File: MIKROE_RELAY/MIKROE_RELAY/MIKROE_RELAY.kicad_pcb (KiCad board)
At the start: 2 copper layers, 32.7 x 53.5 mm, 24 parts, among them J1 RELAY1, J2 RELAY2, J3 Screw_Terminal_01x04, K1 SRD-05VDC-SL-C, K2 SRD-05VDC-SL-C, Q1 Q_NMOS_Depletion_GSD, Q2 Q_NMOS_Depletion_GSD, U2 B0505S-2WR3, U3 PC817, U4 PC817

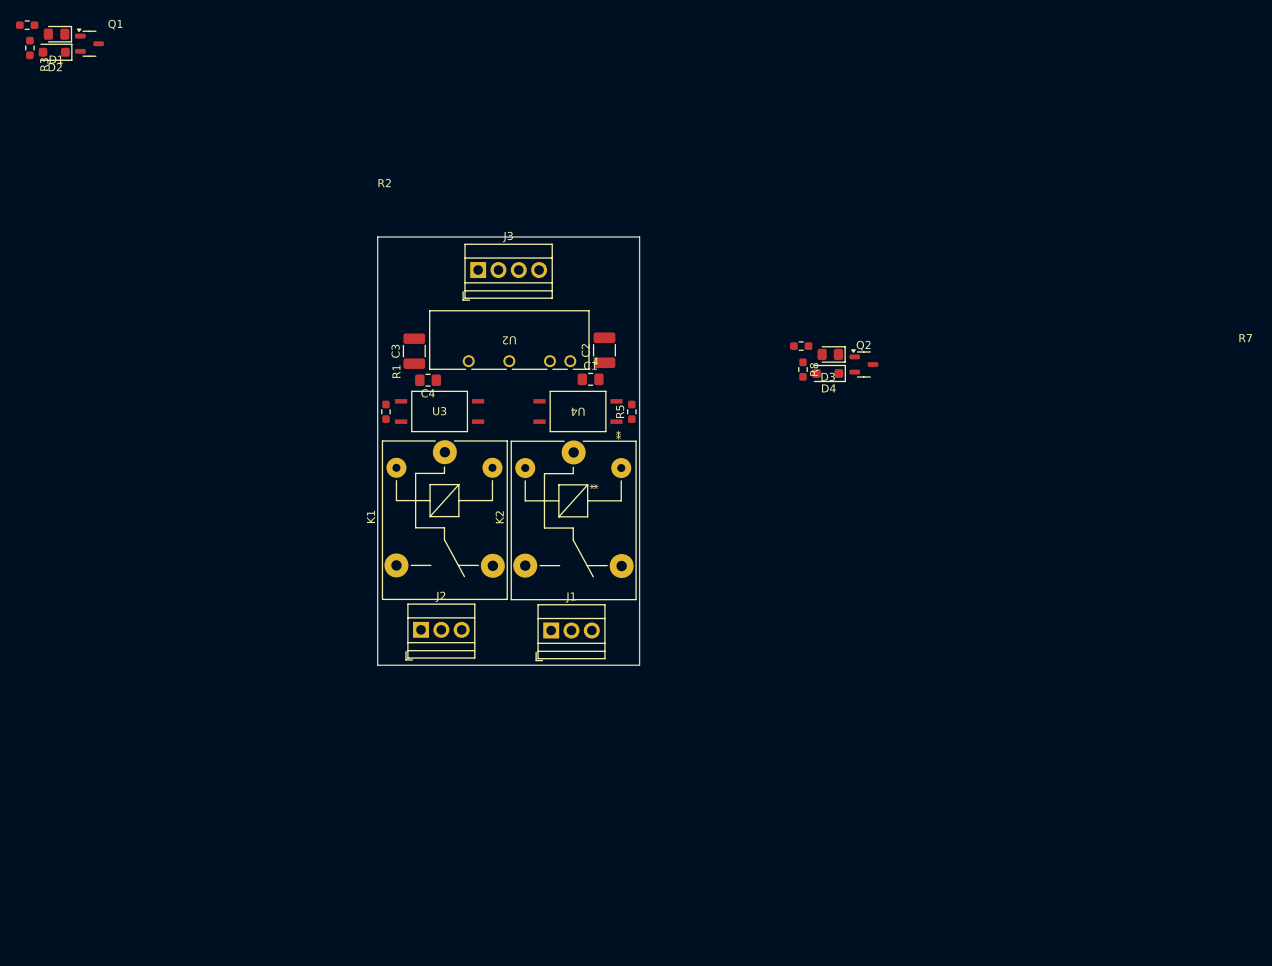
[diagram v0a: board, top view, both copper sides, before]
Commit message: -relay update traces
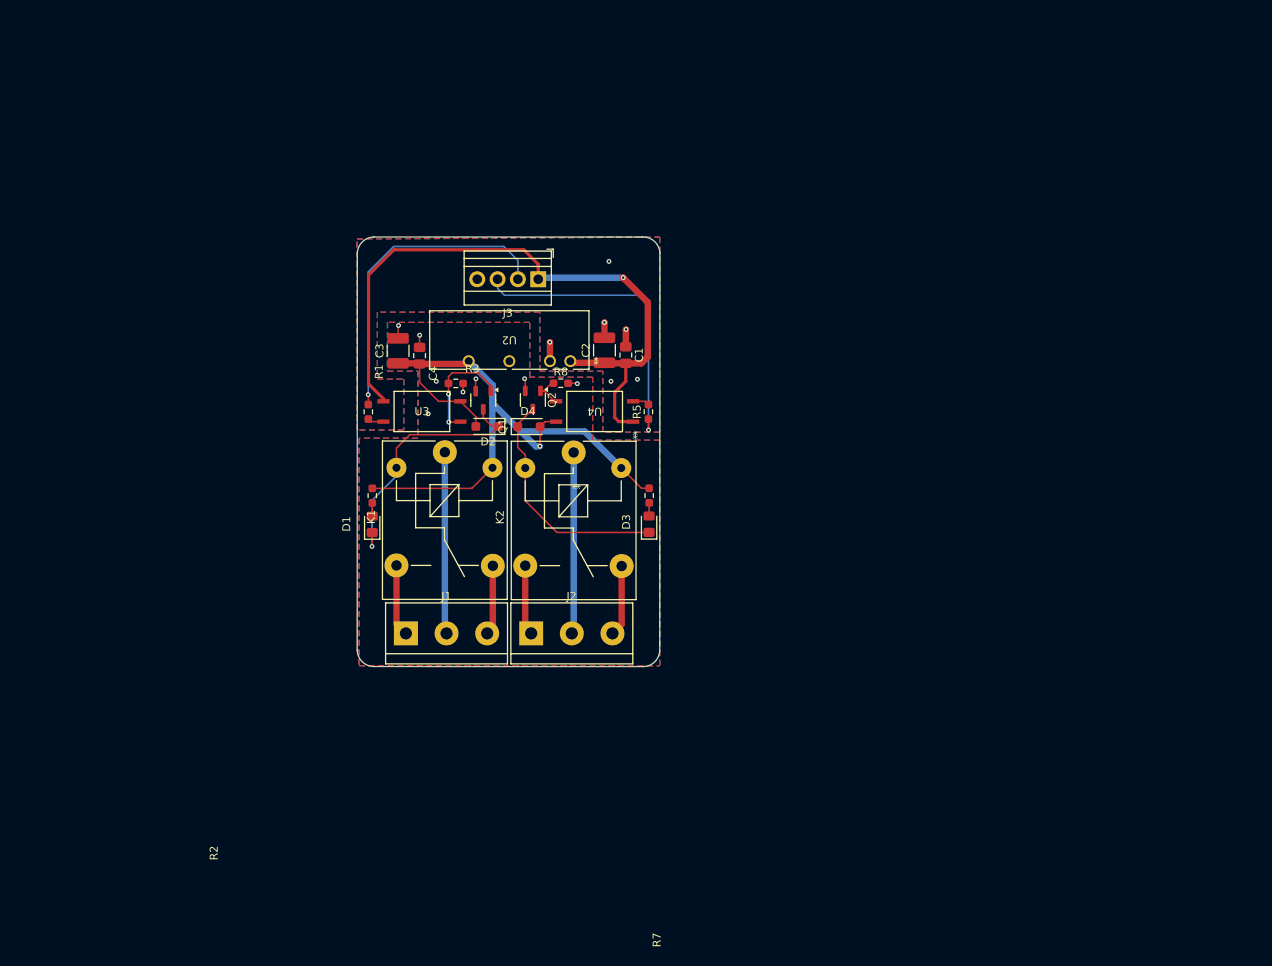
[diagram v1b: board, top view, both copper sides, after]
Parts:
- J1, J2: footprint TerminalBlock:TerminalBlock_Xinya_XY308-2.54-3P_1x03_P2.54mm_Horizontal -> TerminalBlock:TerminalBlock_bornier-3_P5.08mm
- moved R2 72.9 mm to (107.8, 69.2), turned to -90 degrees
- moved D1 72.9 mm to (107.8, 72.8), turned to 90 degrees
- moved D2 71.5 mm to (122.2, 60.5)
- moved R3 67.8 mm to (118.3, 55.1), turned to 0 degrees
- moved Q1 66.4 mm to (121.7, 57.2), turned to -90 degrees
- moved Q2 41.6 mm to (127.9, 57.2), turned to -90 degrees
- moved D4 37.9 mm to (127.4, 60.5), turned to 0 degrees
- moved D3 31.0 mm to (142.4, 72.7), turned to 90 degrees
- moved R8 30.3 mm to (131.4, 55.1), turned to 0 degrees
- moved R7 26.6 mm to (142.4, 69.2), turned to -90 degrees
- moved J1 18.2 mm to (112.0, 86.4)
- moved J2 13.8 mm to (127.7, 86.4)
- moved J3 7.60 mm to (128.6, 42.1), turned to 180 degrees
- moved C1 5.34 mm to (139.5, 51.6), turned to -90 degrees
- moved C4 3.25 mm to (113.7, 51.7), turned to -90 degrees
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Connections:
- J3 pad 1: GNDD -> 5V_ISO
- J3 pad 2: /RE2 -> /RE1
- J3 pad 3: /RE1 -> /RE2
- J3 pad 4: 5V_ISO -> GNDD
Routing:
- net 5V_RLY: track 0.00 -> 86.2 mm, vias 0 -> 1
- net 5V_ISO: track 0.00 -> 83.9 mm, vias 0 -> 1
- net /RE1: track 0.00 -> 39.7 mm, vias 0 -> 1
- net /RE2: track 0.00 -> 37.9 mm, vias 0 -> 1
- net Net-(D1-K): track 0.00 -> 32.5 mm, vias 0 -> 1
- net Net-(D3-K): track 0.00 -> 29.8 mm
- net COM1: track 0.00 -> 22.7 mm
- net COM2: track 0.00 -> 22.7 mm
- net Net-(Q1-G): track 0.00 -> 14.0 mm, vias 0 -> 2
- net NO1: track 0.00 -> 8.99 mm
- net NC2: track 0.00 -> 8.90 mm
- net NO2: track 0.00 -> 8.78 mm
- net NC1: track 0.00 -> 8.74 mm
- net GNDPWR: track 0.00 -> 8.55 mm, vias 0 -> 8
- net GNDD: track 0.00 -> 6.49 mm, vias 0 -> 6
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- added copper zone on B.Cu, net GNDD
- added copper zone on F.Cu, net GNDD
- added copper zone on B.Cu, net GNDPWR
- added copper zone on F.Cu, net GNDPWR
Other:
- board size 32.7 x 53.5 mm -> 37.8 x 53.7 mm

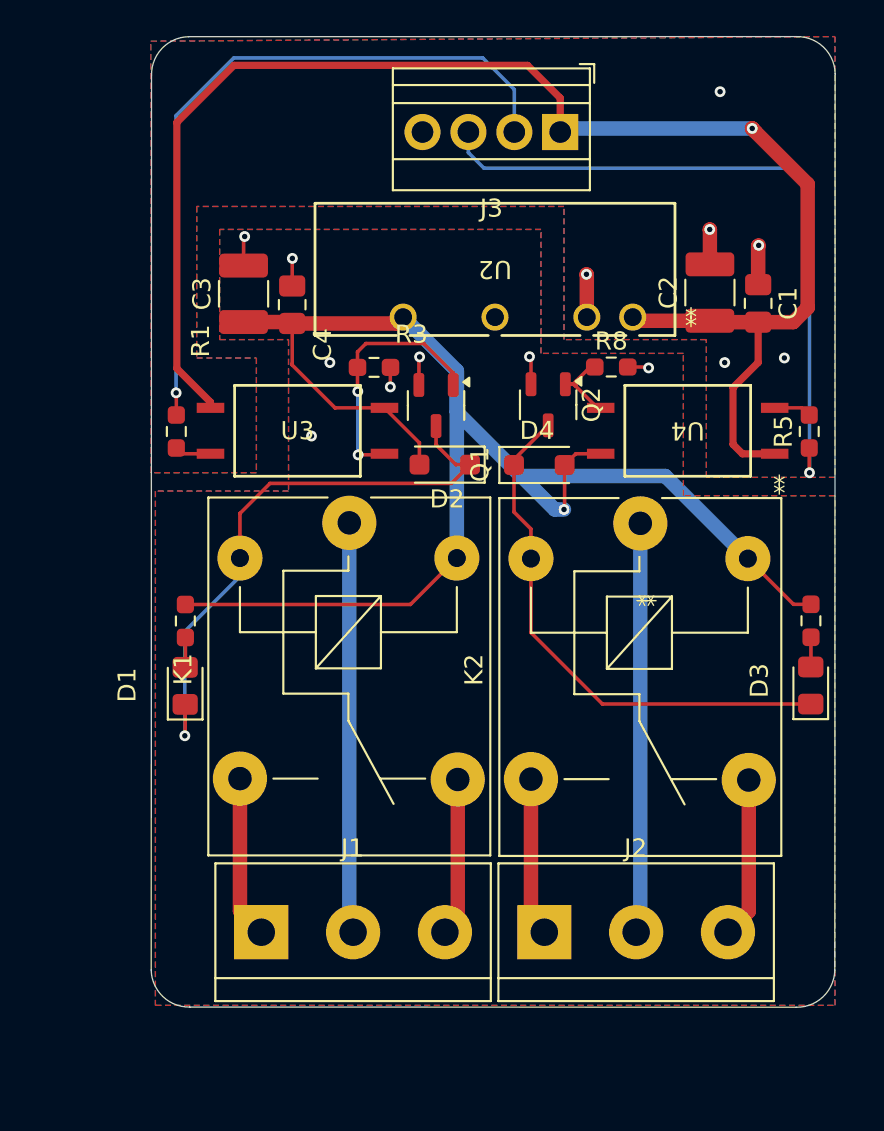
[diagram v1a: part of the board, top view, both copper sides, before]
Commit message: -
updated silk , lacking aesthetic silk
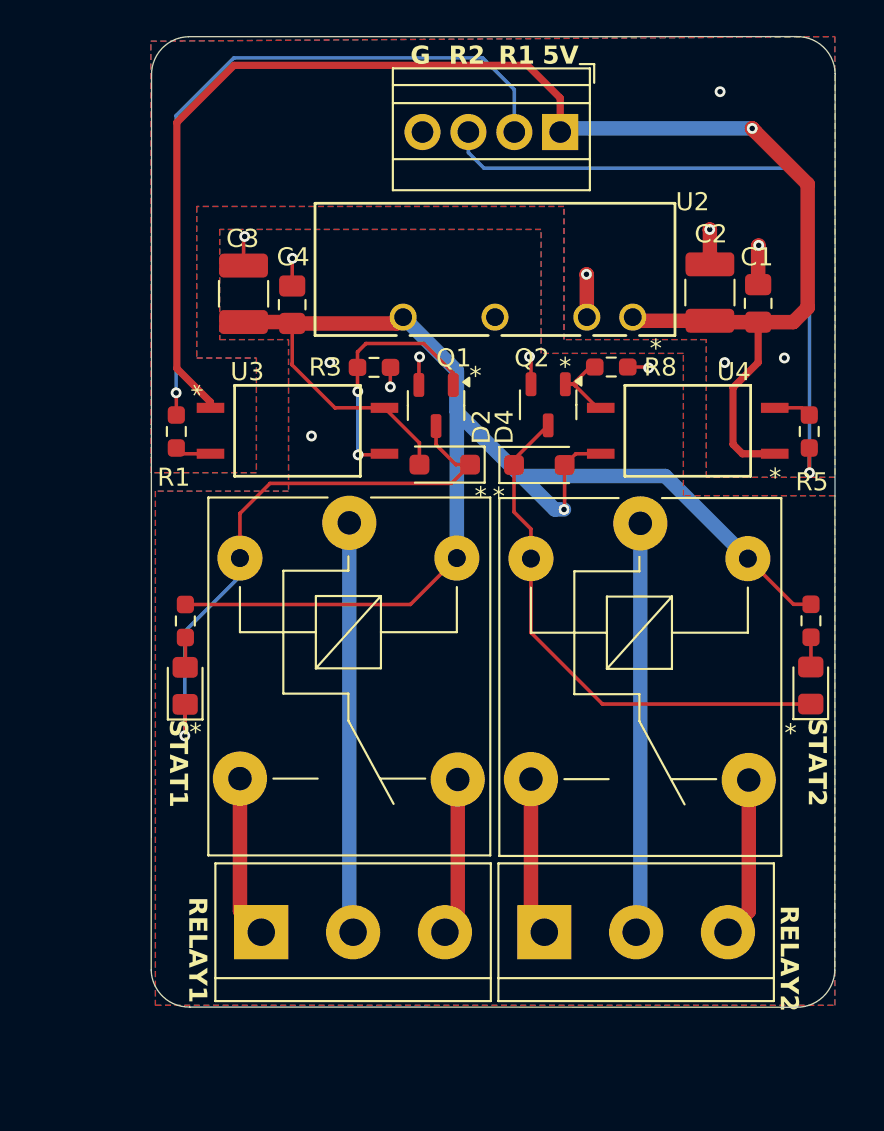
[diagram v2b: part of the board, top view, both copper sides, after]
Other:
- board text added: "*"
- board text added: "5V"
- board text added: "COM1"
- board text added: "COM2"
- board text added: "G"
- board text added: "NC1"
- board text added: "NC2"
- board text added: "NO1"
- board text added: "NO2"
- board text added: "R1"
- board text added: "R2"
- board text added: "RELAY1"
- board text added: "RELAY2"
- board text added: "STAT1"
- board text added: "STAT2"

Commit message: -
updated silk
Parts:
- added G***: LOGO, logo:logo2, F.Cu at (139.5, 48.1)
- added H1: MountingHole, MountingHole:MountingHole_3.2mm_M3_DIN965_Pad, F.Cu at (104.6, 40.1)
- added H2: MountingHole, MountingHole:MountingHole_3.2mm_M3_DIN965_Pad, F.Cu at (145.1, 40.1)
- added H3: MountingHole, MountingHole:MountingHole_3.2mm_M3_DIN965_Pad, F.Cu at (104.6, 87.1)
- added H4: MountingHole, MountingHole:MountingHole_3.2mm_M3_DIN965_Pad, F.Cu at (145.1, 87.1)
- added kibuzzard-6720ECCE: G***, kibuzzard-6720ECCE, F.Cu at (105.7, 77.5)
- added kibuzzard-6720ECE8: G***, kibuzzard-6720ECE8, F.Cu at (144.3, 77.7)
- added kibuzzard-6720EF98: G***, kibuzzard-6720EF98, F.Cu at (125.2, 37.8)
- added kibuzzard-6720F047: G***, kibuzzard-6720F047, B.Cu at (125.2, 37.8)
- added kibuzzard-6720F077: G***, kibuzzard-6720F077, F.Cu at (141.2, 86.3)
- added kibuzzard-6720F077: G***, kibuzzard-6720F077, B.Cu at (141.2, 86.3)
- added kibuzzard-6720F294: G***, kibuzzard-6720F294, F.Cu at (108.6, 86.5)
- added kibuzzard-6720F294: G***, kibuzzard-6720F294, B.Cu at (108.5, 86.5)
- added kibuzzard-6720F424: G***, kibuzzard-6720F424, B.Cu at (112.1, 89.4)
- added kibuzzard-6720F448: G***, kibuzzard-6720F448, B.Cu at (122.3, 89.4)
- added kibuzzard-6720F477: G***, kibuzzard-6720F477, B.Cu at (127.5, 89.4)
- added kibuzzard-6720F484: G***, kibuzzard-6720F484, B.Cu at (138.2, 89.4)
- added kibuzzard-6720F4CB: G***, kibuzzard-6720F4CB, B.Cu at (117.2, 89.4)
- added kibuzzard-6720F4E3: G***, kibuzzard-6720F4E3, B.Cu at (132.9, 89.4)
- added kibuzzard-6720F54C: G***, kibuzzard-6720F54C, F.Cu at (102.5, 72.9)
- added kibuzzard-6720F708: G***, kibuzzard-6720F708, F.Cu at (103.4, 49.0)
- moved R2 2.17 mm to (105.7, 69.2)
- moved D1 2.16 mm to (105.7, 72.8)
- moved D3 1.84 mm to (144.3, 72.7)
- moved R7 1.83 mm to (144.3, 69.2)
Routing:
- net 5V_ISO: track 83.9 -> 79.4 mm
- net 5V_RLY: track 86.2 -> 90.2 mm
- net /RE1: track 39.7 -> 36.5 mm
- net Net-(D3-K): track 29.8 -> 31.6 mm
- net Net-(D1-K): track 32.5 -> 33.6 mm
- net GNDD: vias 6 -> 8
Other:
- board size 37.8 x 53.7 mm -> 47.4 x 53.7 mm
- board text removed: "5V"
- board text removed: "COM1"
- board text removed: "COM2"
- board text removed: "G"
- board text removed: "NC1"
- board text removed: "NC2"
- board text removed: "NO1"
- board text removed: "NO2"
- board text removed: "R1"
- board text removed: "R2"
- board text removed: "RELAY1"
- board text removed: "RELAY2"
- board text removed: "STAT1"
- board text removed: "STAT2"

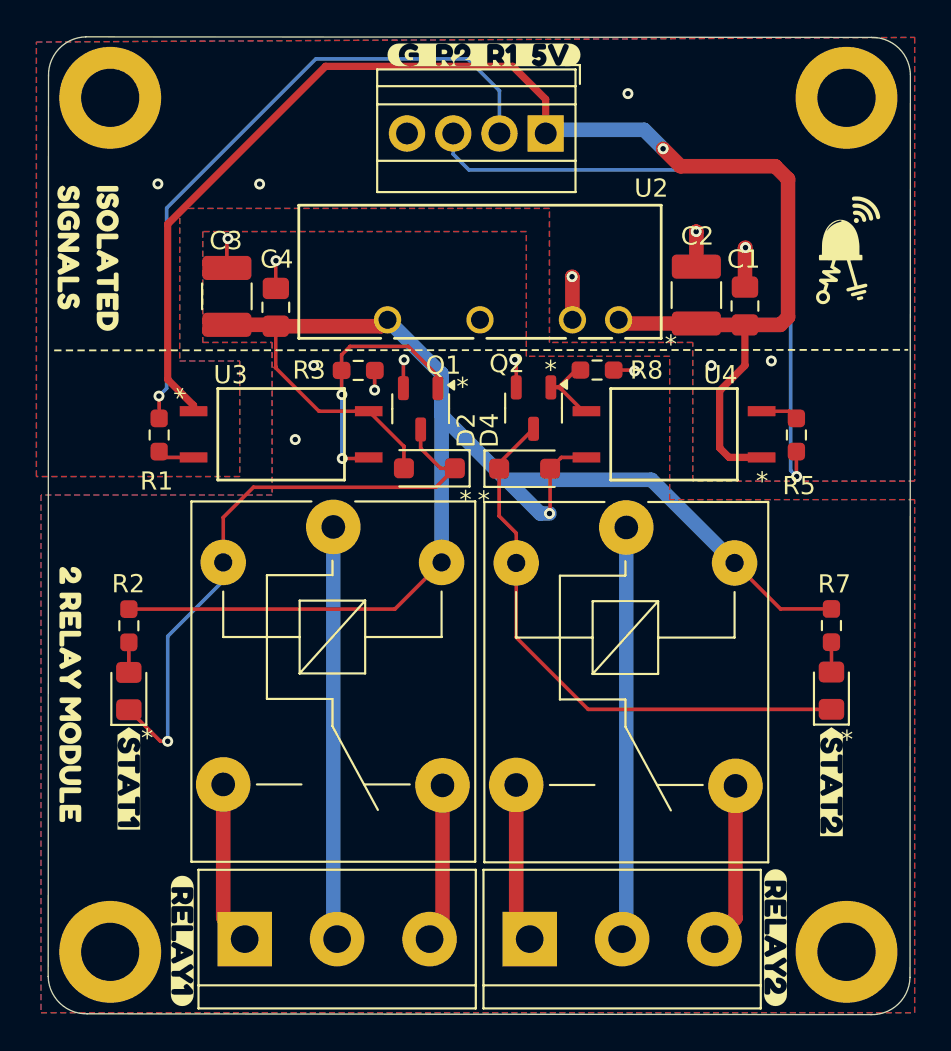
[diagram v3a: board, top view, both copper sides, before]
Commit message: Fixed Silk Screen
Minor Adjustments
1. Silk Screens
2. Swapped Relay Pin Signals
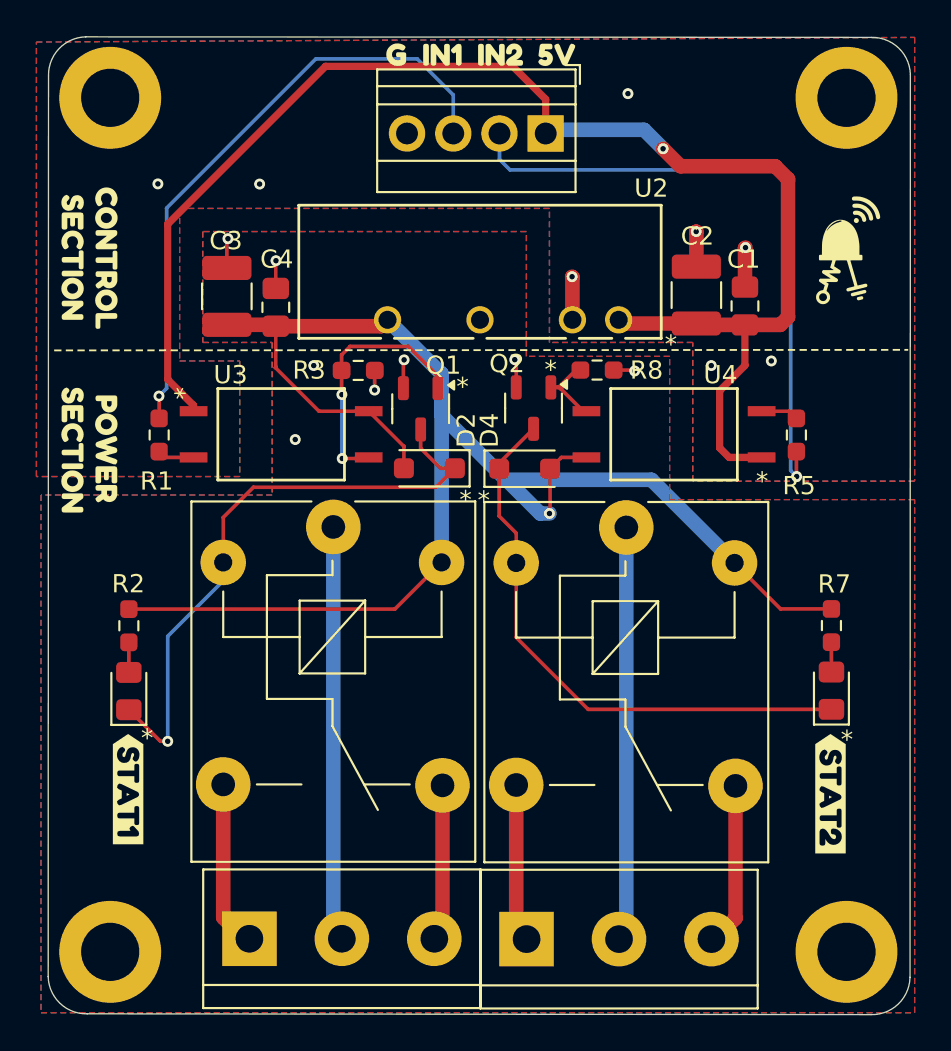
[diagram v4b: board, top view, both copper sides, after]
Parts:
- removed kibuzzard-6720ECCE: G***, kibuzzard-6720ECCE
- removed kibuzzard-6720ECE8: G***, kibuzzard-6720ECE8
- removed kibuzzard-6720EF98: G***, kibuzzard-6720EF98
- removed kibuzzard-6720F047: G***, kibuzzard-6720F047
- removed kibuzzard-6720F077 (x2): G***, kibuzzard-6720F077
- removed kibuzzard-6720F294 (x2): G***, kibuzzard-6720F294
- removed kibuzzard-6720F424: G***, kibuzzard-6720F424
- removed kibuzzard-6720F448: G***, kibuzzard-6720F448
- removed kibuzzard-6720F477: G***, kibuzzard-6720F477
- removed kibuzzard-6720F484: G***, kibuzzard-6720F484
- removed kibuzzard-6720F4CB: G***, kibuzzard-6720F4CB
- removed kibuzzard-6720F4E3: G***, kibuzzard-6720F4E3
- removed kibuzzard-6720F54C: G***, kibuzzard-6720F54C
- removed kibuzzard-6720F708: G***, kibuzzard-6720F708
- added kibuzzard-672479F1: G***, kibuzzard-672479F1, F.Cu at (103.5, 49.0)
- added kibuzzard-67247A26: G***, kibuzzard-67247A26, F.Cu at (103.5, 59.5)
- added kibuzzard-67247B67: G***, kibuzzard-67247B67, F.Cu at (144.2, 78.4)
- added kibuzzard-67247B7C: G***, kibuzzard-67247B7C, F.Cu at (105.6, 78.1)
- added kibuzzard-67247F02: G***, kibuzzard-67247F02, B.Cu at (132.9, 89.4)
- added kibuzzard-67247F27: G***, kibuzzard-67247F27, B.Cu at (138.1, 89.4)
- added kibuzzard-67247F36: G***, kibuzzard-67247F36, B.Cu at (127.6, 89.4)
- added kibuzzard-67247F5C: G***, kibuzzard-67247F5C, B.Cu at (122.2, 89.4)
- added kibuzzard-67247F6F: G***, kibuzzard-67247F6F, B.Cu at (117.2, 89.4)
- added kibuzzard-67247F7C: G***, kibuzzard-67247F7C, B.Cu at (112.2, 89.4)
- added kibuzzard-67248361: G***, kibuzzard-67248361, F.Cu at (125.0, 37.8)
- added kibuzzard-6724836D: G***, kibuzzard-6724836D, B.Cu at (125.0, 39.9)
- moved J1 0.26 mm to (112.3, 86.4)
- moved J2 0.17 mm to (127.5, 86.4)
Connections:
- J3 pad 2: /RE1 -> /RE2
- J3 pad 3: /RE2 -> /RE1
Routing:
- net /RE1: track 36.5 -> 33.7 mm
- net /RE2: track 37.9 -> 35.5 mm
